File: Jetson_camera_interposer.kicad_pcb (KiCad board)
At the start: 6 copper layers, 71.1 x 75 mm, 49 parts, among them J1 QSH-060-01-L-D-A, J2 QTH-060-01-L-D-A, J21 Conn_01x01, J22 Conn_01x01, J23 Conn_01x01, J24 Conn_01x01, J25 Conn_01x01, J26 Conn_01x01, J3 Conn_01x01, J4 Conn_01x01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

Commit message: more schematic editing
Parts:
- removed R1, R10, R2, R3, R4, R5, R6, R7, R8, R9: 0, TX2_Footprints:R_0805
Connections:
- J1 pad 1: /MUXED_1_D0_P -> /CSI0_D0_P
- J1 pad 13: /MUXED_1_D1_P -> /CSI0_D1_P
- J1 pad 14: /MUXED_1_D3_P -> /CSI1_D1_P
- J1 pad 15: /MUXED_1_D1_N -> /CSI0_D1_N
- J1 pad 16: /MUXED_1_D3_N -> /CSI1_D1_N
- J1 pad 19: (no net) -> /CSI2_D0_P
- J1 pad 2: /MUXED_1_D2_P -> /CSI1_D0_P
- J1 pad 20: (no net) -> /CSI3_D0_P
- J1 pad 21: (no net) -> /CSI2_D0_N
- J1 pad 22: (no net) -> /CSI3_D0_N
- J1 pad 25: (no net) -> /CSI2_CLK_P
- J1 pad 26: (no net) -> /CSI3_CLK_P
- J1 pad 27: (no net) -> /CSI2_CLK_N
- J1 pad 28: (no net) -> /CSI3_CLK_N
- J1 pad 3: /MUXED_1_D0_N -> /CSI0_D0_N
- J1 pad 31: (no net) -> /CSI2_D1_P
- J1 pad 32: (no net) -> /CSI3_D1_P
- J1 pad 33: (no net) -> /CSI2_D1_N
- J1 pad 34: (no net) -> /CSI3_D1_N
- J1 pad 37: (no net) -> /CSI4_D0_P
- J1 pad 38: (no net) -> /CSI5_D0_P
- J1 pad 39: (no net) -> /CSI4_D0_N
- J1 pad 4: /MUXED_1_D2_N -> /CSI1_D0_N
- J1 pad 40: (no net) -> /CSI5_D0_N
- J1 pad 43: (no net) -> /CSI4_CLK_P
- J1 pad 44: (no net) -> /CSI5_CLK_P
- J1 pad 45: (no net) -> /CSI4_CLK_N
- J1 pad 46: (no net) -> /CSI5_CLK_N
- J1 pad 49: (no net) -> /CSI4_D1_P
- J1 pad 50: (no net) -> /CSI5_D1_P
- J1 pad 51: (no net) -> /CSI4_D1_N
- J1 pad 52: (no net) -> /CSI5_D1_N
- J1 pad 7: /MUXED_1_CLK_P -> /CSI0_CLK_P
- J1 pad 9: /MUXED_1_CLK_N -> /CSI0_CLK_N
- J2 pad 19: (no net) -> /CSI2_D0_P
- J2 pad 20: (no net) -> /CSI3_D0_P
- J2 pad 21: (no net) -> /CSI2_D0_N
- J2 pad 22: (no net) -> /CSI3_D0_N
- J2 pad 25: (no net) -> /CSI2_CLK_P
- J2 pad 26: (no net) -> /CSI3_CLK_P
- J2 pad 27: (no net) -> /CSI2_CLK_N
- J2 pad 28: (no net) -> /CSI3_CLK_N
- J2 pad 31: (no net) -> /CSI2_D1_P
- J2 pad 32: (no net) -> /CSI3_D1_P
- J2 pad 33: (no net) -> /CSI2_D1_N
- J2 pad 34: (no net) -> /CSI3_D1_N
- J2 pad 37: (no net) -> /CSI4_D0_P
- J2 pad 38: (no net) -> /CSI5_D0_P
- J2 pad 39: (no net) -> /CSI4_D0_N
- J2 pad 40: (no net) -> /CSI5_D0_N
- J2 pad 43: (no net) -> /CSI4_CLK_P
- J2 pad 44: (no net) -> /CSI5_CLK_P
- J2 pad 45: (no net) -> /CSI4_CLK_N
- J2 pad 46: (no net) -> /CSI5_CLK_N
- J2 pad 49: (no net) -> /CSI4_D1_P
- J2 pad 50: (no net) -> /CSI5_D1_P
- J2 pad 51: (no net) -> /CSI4_D1_N
- J2 pad 52: (no net) -> /CSI5_D1_N
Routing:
- net /CSI2_D0_N: track 0.00 -> 158.8 mm
- net /MUXED_1_D2_P: track 96.5 -> 0.00 mm
- net /CSI1_D0_P: track 29.9 -> 126.4 mm
- net /CSI1_D0_N: track 30.0 -> 126.4 mm
- net /MUXED_1_D2_N: track 96.4 -> 0.00 mm
- net /CSI0_D1_P: track 43.3 -> 126.5 mm, vias 1 -> 3
- net /MUXED_1_D1_P: track 83.2 -> 0.00 mm, vias 2 -> 0
- net /CSI0_D1_N: track 43.3 -> 126.5 mm, vias 1 -> 3
- net /MUXED_1_D1_N: track 83.2 -> 0.00 mm, vias 2 -> 0
- net /CSI1_D1_N: track 26.7 -> 106.1 mm
- net /MUXED_1_D3_N: track 79.4 -> 0.00 mm
- net /CSI1_D1_P: track 26.7 -> 106.0 mm
- net /MUXED_1_D3_P: track 79.3 -> 0.00 mm
- net /MUXED_1_CLK_P: track 79.2 -> 0.00 mm
- net /CSI0_CLK_P: track 47.3 -> 126.5 mm
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
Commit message: cleaned PCB
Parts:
- moved J6 76.8 mm to (21.7, 116.0)
- moved J25 68.3 mm to (37.7, 105.7)
- moved J26 68.3 mm to (38.5, 109.1)
- moved J4 68.3 mm to (43.6, 112.9)
- moved J22 68.3 mm to (27.0, 99.5)
- moved J23 68.3 mm to (28.1, 106.7)
- moved J24 68.3 mm to (27.7, 114.8)
- moved J3 68.3 mm to (27.5, 117.4)
- moved J5 68.3 mm to (43.6, 121.0)
- moved J21 63.8 mm to (31.4, 96.8)
- moved GND3 17.4 mm to (141.6, 53.9)
- moved GND4 16.6 mm to (120.4, 54.3)
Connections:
- J1 pad 10: (no net) -> /CSI1_CLK_N
- J1 pad 72: (no net) -> /I2S3_CLK
- J1 pad 74: (no net) -> /I2S3_LRCLK
- J1 pad 76: (no net) -> /I2S3_SDIN
- J1 pad 78: (no net) -> /I2S3_SDOUT
- J1 pad 8: (no net) -> /CSI1_CLK_P
- J1 pad 87: (no net) -> /CAM_I2C2_SCL
- J1 pad 88: (no net) -> /CAM1_MCLK
- J1 pad 89: (no net) -> /CAM_I2C2_SDA
- J1 pad 90: (no net) -> /CAM1_PWDN
- J1 pad 92: (no net) -> /CAM1_RST_L
- J1 pad 94: (no net) -> /CAM2_MCLK
- J1 pad 96: (no net) -> /CAM2_PWDN
- J1 pad 98: (no net) -> /CAM2_RST
- J2 pad 10: (no net) -> /CSI1_CLK_N
- J2 pad 72: (no net) -> /I2S3_CLK
- J2 pad 74: (no net) -> /I2S3_LRCLK
- J2 pad 76: (no net) -> /I2S3_SDIN
- J2 pad 78: (no net) -> /I2S3_SDOUT
- J2 pad 8: (no net) -> /CSI1_CLK_P
- J2 pad 87: (no net) -> /CAM_I2C2_SCL
- J2 pad 88: (no net) -> /CAM1_MCLK
- J2 pad 89: (no net) -> /CAM_I2C2_SDA
- J2 pad 90: (no net) -> /CAM1_PWDN
- J2 pad 92: (no net) -> /CAM1_RST_L
- J2 pad 94: (no net) -> /CAM2_MCLK
- J2 pad 96: (no net) -> /CAM2_PWDN
- J2 pad 98: (no net) -> /CAM2_RST
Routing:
- net /CSI2_D0_N: track 158.8 -> 0.00 mm
- net /CSI0_D1_P: track 126.5 -> 0.00 mm, vias 3 -> 0
- net /CSI0_D1_N: track 126.5 -> 0.00 mm, vias 3 -> 0
- net /CSI0_CLK_P: track 126.5 -> 0.00 mm, vias 1 -> 0
- net /CSI0_CLK_N: track 126.5 -> 0.00 mm, vias 1 -> 0
- net /CSI1_D0_N: track 126.4 -> 0.00 mm, vias 1 -> 0
- net /CSI1_D0_P: track 126.4 -> 0.00 mm, vias 1 -> 0
- net /CSI0_D0_N: track 120.0 -> 0.00 mm, vias 1 -> 0
- net /CSI0_D0_P: track 118.0 -> 0.00 mm, vias 1 -> 0
- net /CSI1_D1_N: track 106.1 -> 0.00 mm, vias 1 -> 0
- net /CSI1_D1_P: track 106.0 -> 0.00 mm, vias 1 -> 0
- net /I2C_CAM_CLK: track 71.8 -> 0.00 mm, vias 3 -> 0
- net /JETSON_1V8: track 70.2 -> 0.00 mm, vias 4 -> 0
- net /CAM_AF_PWDN: track 65.9 -> 0.00 mm, vias 3 -> 0
- net /I2C_GP0_DAT_1V8: track 64.0 -> 0.00 mm, vias 3 -> 0
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
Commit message: starting layout
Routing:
- net /DVDD_CAM_LV: track 0.00 -> 39.8 mm, vias 0 -> 2
- net /IR_READY: track 0.00 -> 32.1 mm, vias 0 -> 2
- net /CAM_INTR: track 0.00 -> 31.4 mm, vias 0 -> 2
- net /VDD_SYS: track 0.00 -> 30.6 mm, vias 0 -> 2
- net /VDD_3V3: track 0.00 -> 30.5 mm, vias 0 -> 2
- net /VDD_IR: track 0.00 -> 30.3 mm, vias 0 -> 2
- net /I2C_GP0_DAT_1V8: track 0.00 -> 30.3 mm, vias 0 -> 2
- net /I2C_GP0_CLK_1V8: track 0.00 -> 29.8 mm, vias 0 -> 2
- net /IR_TRIGGER: track 0.00 -> 29.5 mm, vias 0 -> 2
- net /VSYS_EN: track 0.00 -> 28.8 mm, vias 0 -> 2
- net /VDD_AF: track 0.00 -> 26.5 mm, vias 0 -> 2
- net /AVDD_CAM: track 0.00 -> 26.4 mm, vias 0 -> 2
- net /JETSON_1V8: track 0.00 -> 26.4 mm, vias 0 -> 2
- net /JETSON_1V2: track 0.00 -> 26.4 mm, vias 0 -> 2
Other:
- net class Power added: clearance 0.254, trace_width 0.254, via_dia 0.254, via_drill 0.2032

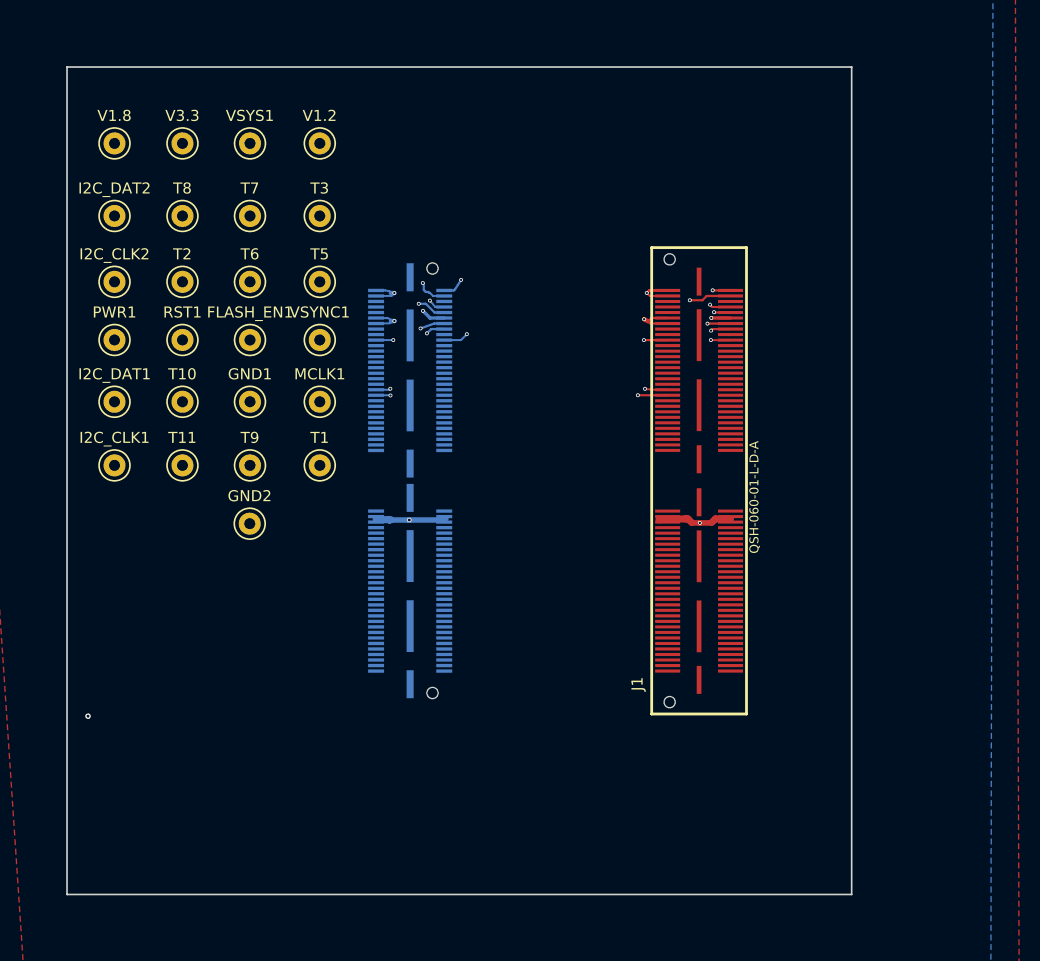
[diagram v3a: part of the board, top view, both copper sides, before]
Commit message: added high-speed lines
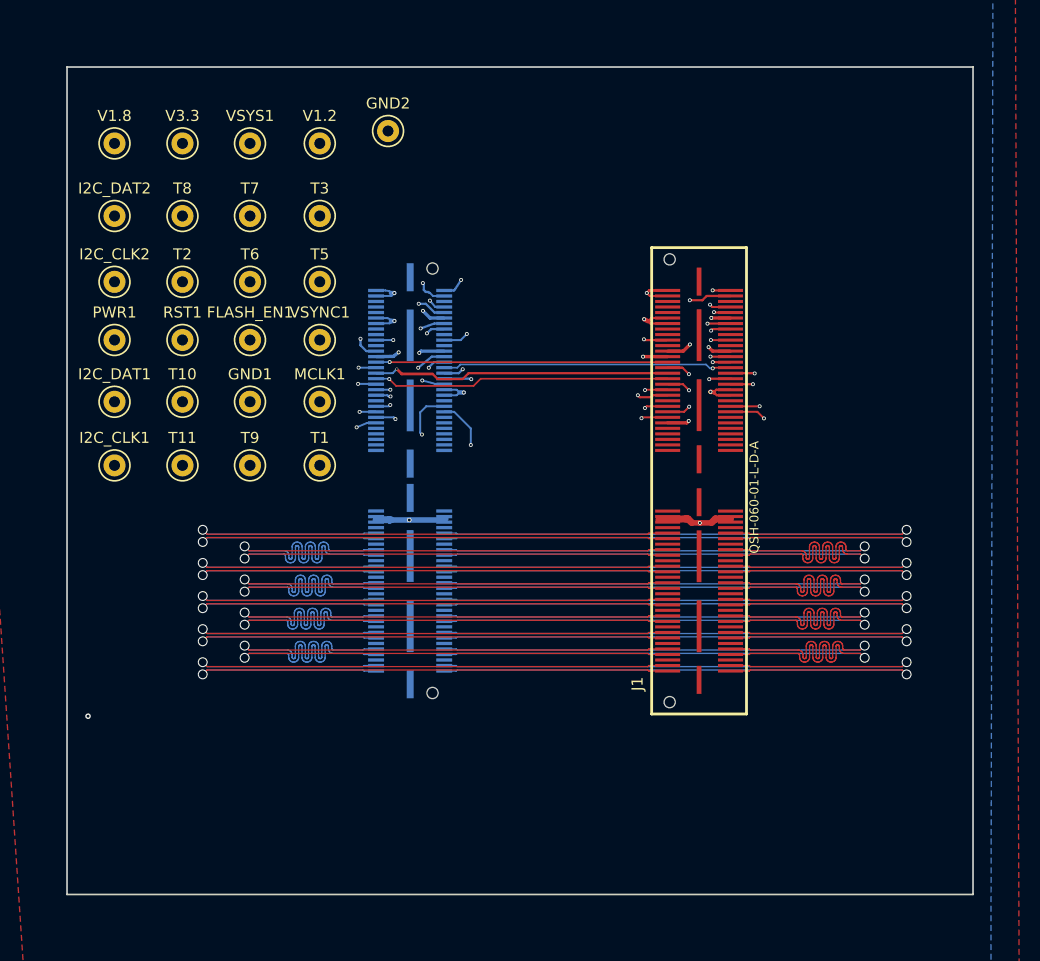
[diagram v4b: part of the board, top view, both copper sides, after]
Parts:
- moved GND2 37.7 mm to (118.0, 71.8)
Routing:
- net /CSI2_CLK_N: track 0.00 -> 58.3 mm, vias 0 -> 1
- net /CSI0_D1_N: track 0.00 -> 58.3 mm, vias 0 -> 1
- net /CSI0_D0_P: track 0.00 -> 58.3 mm, vias 0 -> 1
- net /CSI4_D0_P: track 0.00 -> 58.3 mm, vias 0 -> 1
- net /CSI4_D0_N: track 0.00 -> 58.3 mm, vias 0 -> 1
- net /CSI2_CLK_P: track 0.00 -> 58.3 mm, vias 0 -> 1
- net /CSI0_D1_P: track 0.00 -> 58.3 mm, vias 0 -> 1
- net /CSI0_D0_N: track 0.00 -> 58.3 mm, vias 0 -> 1
- net /CSI4_D1_N: track 0.00 -> 58.3 mm, vias 0 -> 1
- net /CSI4_D1_P: track 0.00 -> 58.3 mm, vias 0 -> 1
- net /CSI5_CLK_P: track 0.00 -> 58.3 mm, vias 0 -> 1
- net /CSI3_D0_P: track 0.00 -> 58.3 mm, vias 0 -> 1
- net /CSI3_D1_P: track 0.00 -> 58.3 mm, vias 0 -> 1
- net /CSI1_CLK_P: track 0.00 -> 58.3 mm, vias 0 -> 1
- net /CSI5_CLK_N: track 0.00 -> 58.3 mm, vias 0 -> 1
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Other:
- board size 71.1 x 75 mm -> 82.1 x 75 mm
- net class MIPI_DIFF: clearance 0.1524 -> 0.2032; via_dia 0.3556 -> 0.9; via_drill 0.2032 -> 0.7

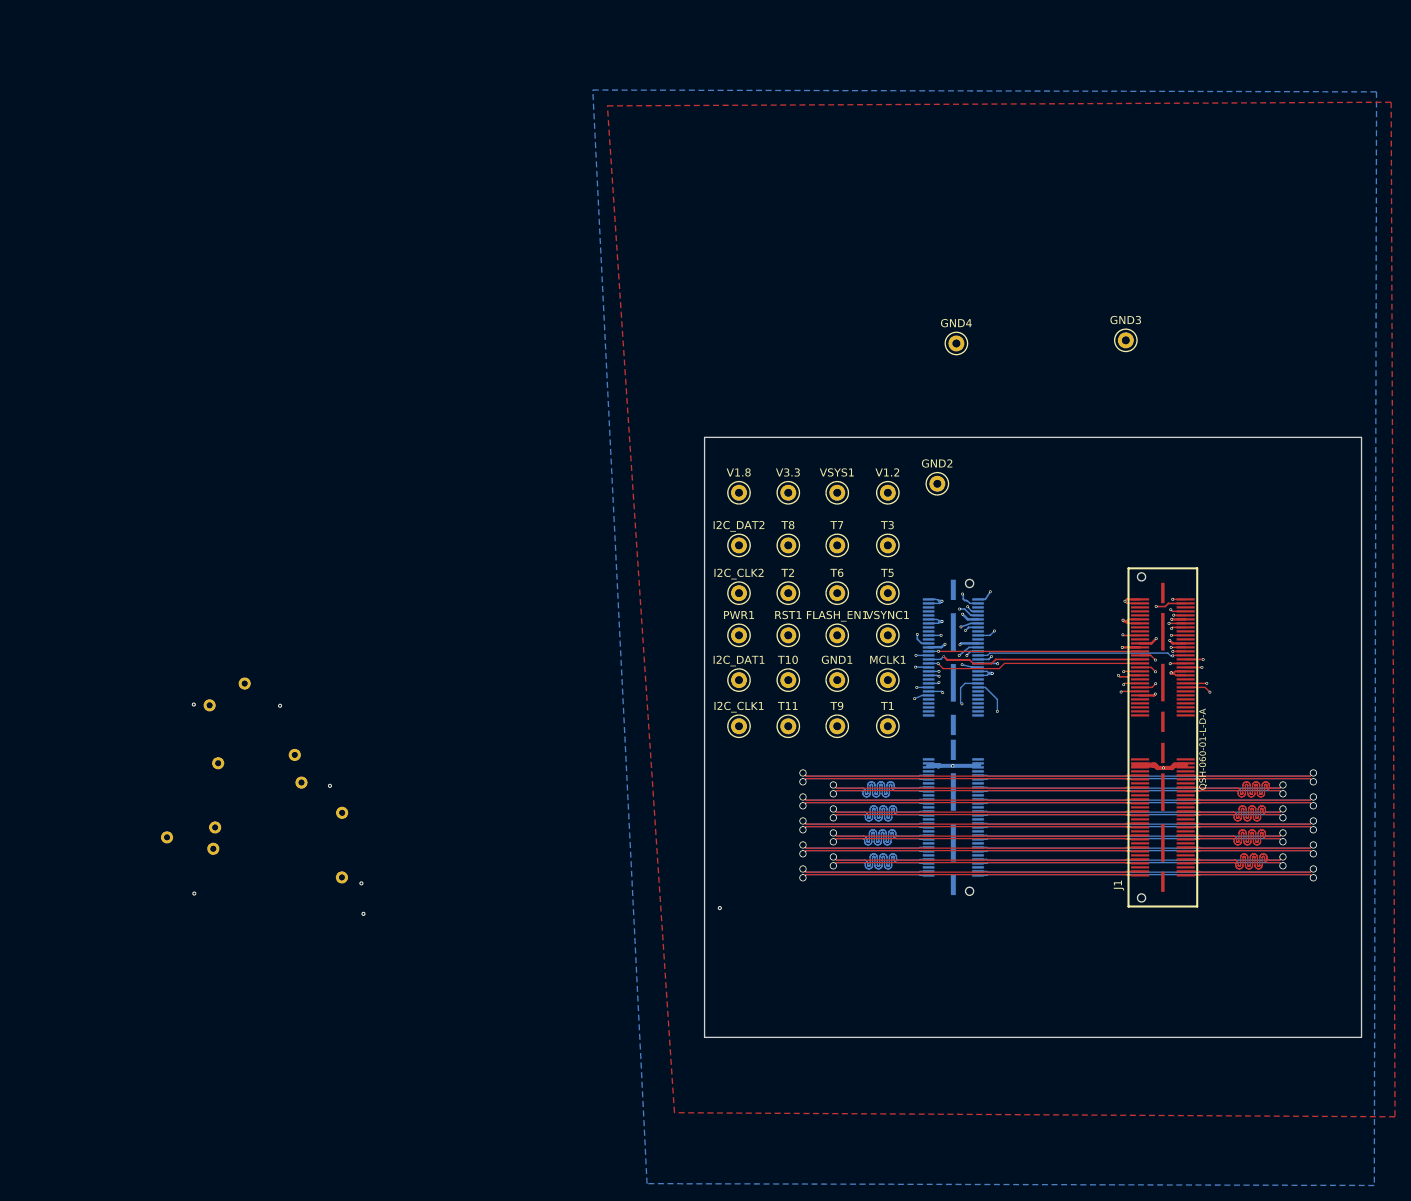
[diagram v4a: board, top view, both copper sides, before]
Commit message: Added vias, before pin-header connector
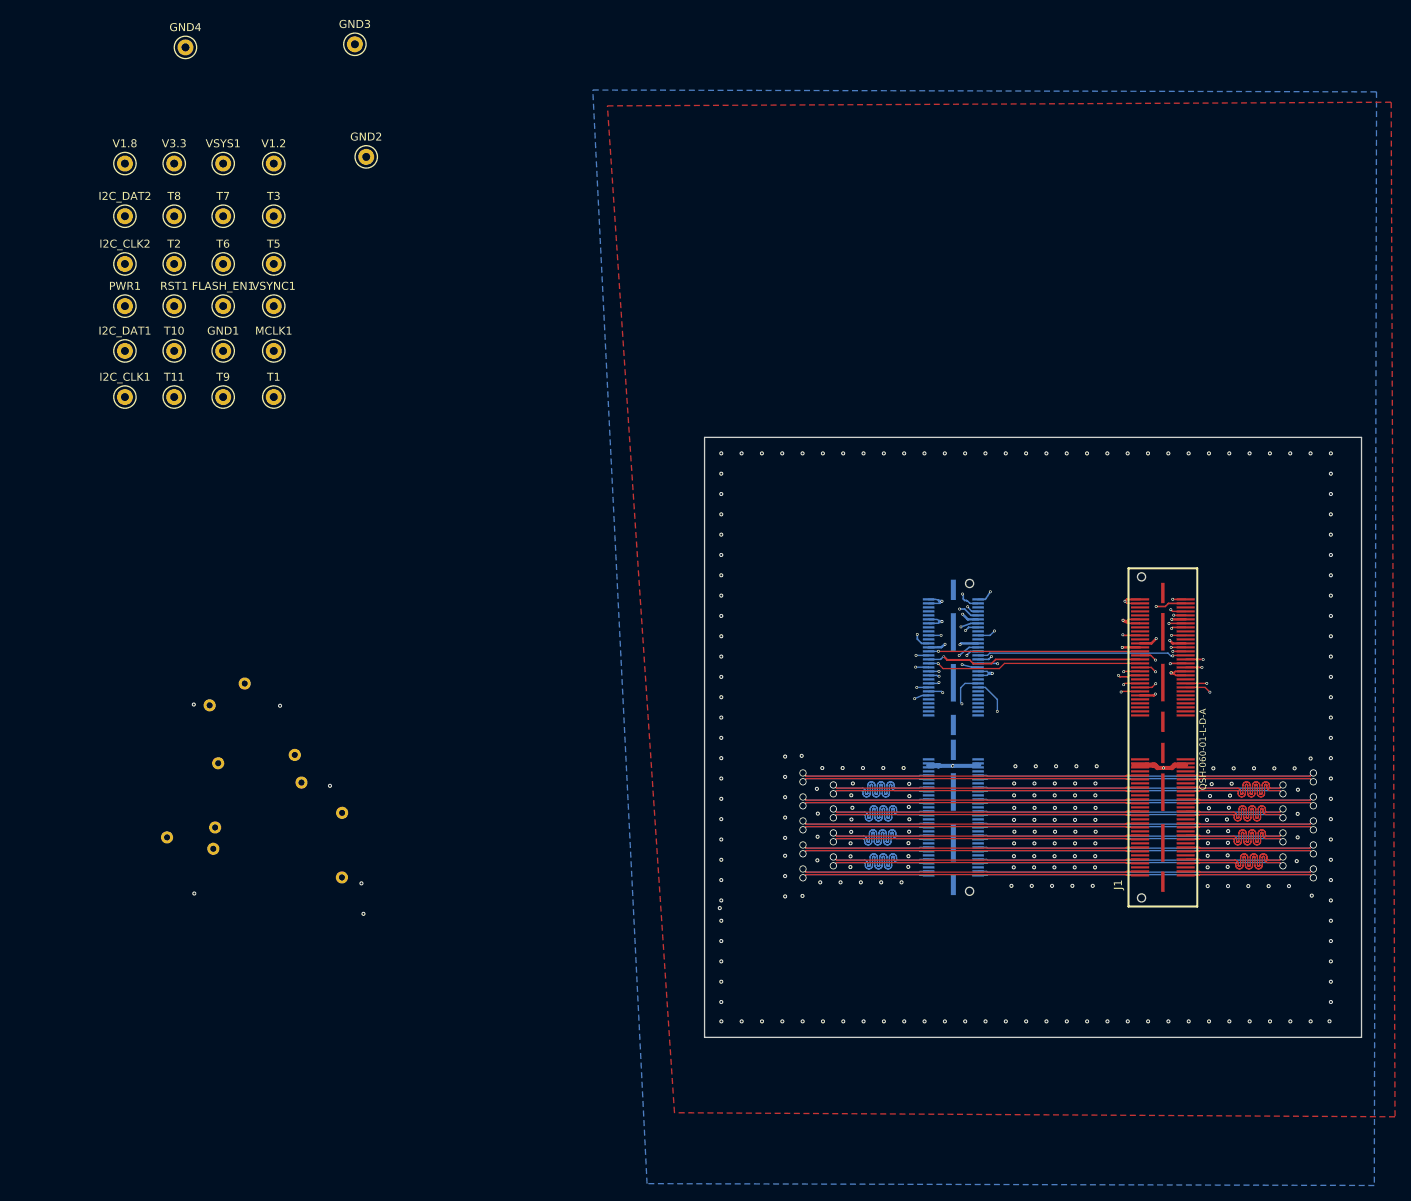
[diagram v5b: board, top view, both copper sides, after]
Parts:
- moved GND3 103.2 mm to (45.2, 16.9)
- moved GND4 103.2 mm to (24.0, 17.3)
- moved RST1 87.1 mm to (22.6, 49.6)
- moved T1 87.1 mm to (35.1, 61.0)
- moved T11 87.1 mm to (22.6, 61.0)
- moved T2 87.1 mm to (22.6, 44.3)
- moved T3 87.1 mm to (35.1, 38.4)
- moved T5 87.1 mm to (35.1, 44.3)
- moved T8 87.1 mm to (22.6, 38.4)
- moved VSYNC1 87.1 mm to (35.1, 49.6)
- moved FLASH_EN1 87.1 mm to (28.7, 49.6)
- moved GND1 87.1 mm to (28.7, 55.2)
- moved I2C_CLK1 87.1 mm to (16.4, 61.0)
- moved I2C_CLK2 87.1 mm to (16.4, 44.3)
- moved I2C_DAT1 87.1 mm to (16.4, 55.2)
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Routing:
- net /DVDD_CAM_LV: track 39.8 -> 42.0 mm
- net Earth: vias 7 -> 245
